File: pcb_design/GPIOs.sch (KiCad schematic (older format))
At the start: 8 parts

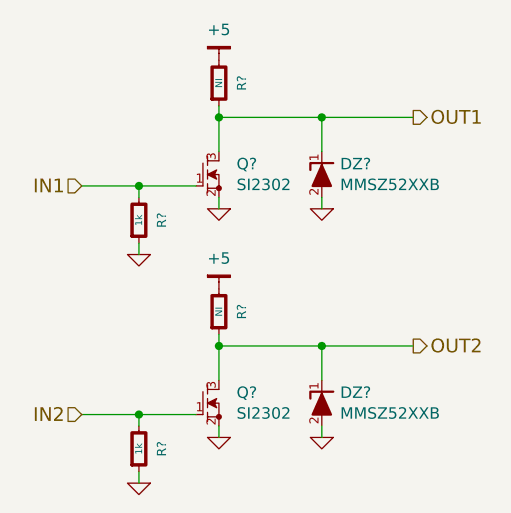
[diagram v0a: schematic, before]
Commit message: Fixed power supply inductor footprints in the layout
Signed-off-by: Marcos Chaparro <mchaparro@paltatech.com>
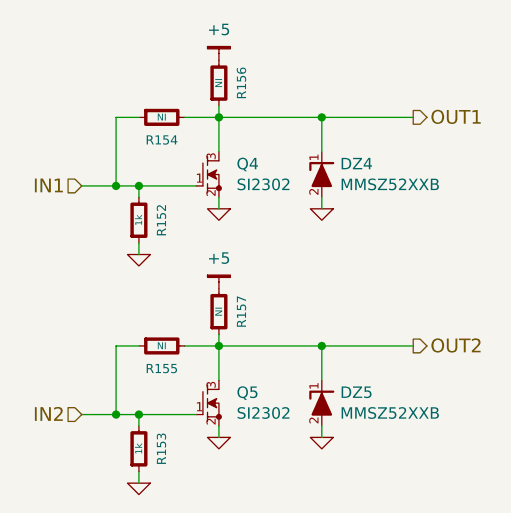
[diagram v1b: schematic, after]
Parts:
- added R154, R155: NI, IPC7351-Nominal:RESC1608X50, symbol R-0603
- gave numbers to parts that had none: 8
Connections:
- net IN1: now also R154.1
- net IN2: now also R155.1
- net OUT1: now also R154.2
- net OUT2: now also R155.2
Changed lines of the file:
@@
 $EndDescr
 $Comp
-L 2N7002K Q?
+L 2N7002K Q5
 U 1 1 594CFF0C
 P 5450 4600
-F 0 "Q?" H 5577 4646 50  0000 L CNN
+F 0 "Q5" H 5577 4646 50  0000 L CNN
 F 1 "SI2302" H 5577 4555 50  0000 L CNN
 F 2 "smd-semi:SOT-23" H 5450 4350 50  0001 C CNN
@@
 $EndComp
 $Comp
-L 2N7002K Q?
+L 2N7002K Q4
 U 1 1 594CFF16
 P 5450 3600
-F 0 "Q?" H 5577 3646 50  0000 L CNN
+F 0 "Q4" H 5577 3646 50  0000 L CNN
 F 1 "SI2302" H 5577 3555 50  0000 L CNN
 F 2 "smd-semi:SOT-23" H 5450 3350 50  0001 C CNN
@@
 P 5500 3750
 AR Path="/594CFF1D" Ref="#PWR?"  Part="1"
-AR Path="/594CEEA9/594CFF1D" Ref="#PWR?"  Part="1"
-F 0 "#PWR?" H 5500 3750 30  0001 C CNN
+AR Path="/594CEEA9/594CFF1D" Ref="#PWR0230"  Part="1"
+F 0 "#PWR0230" H 5500 3750 30  0001 C CNN
 F 1 "GND" H 5500 3680 30  0001 C CNN
 F 2 "" H 5500 3750 60  0000 C CNN
@@
 	5500 4300 5500 4500
 Wire Wire Line
-	5500 4350 6350 4350
+	5350 4350 6350 4350
 Wire Wire Line
 	4900 3650 5400 3650
@@
 P 5500 4750
 AR Path="/594CFF2B" Ref="#PWR?"  Part="1"
-AR Path="/594CEEA9/594CFF2B" Ref="#PWR?"  Part="1"
-F 0 "#PWR?" H 5500 4750 30  0001 C CNN
+AR Path="/594CEEA9/594CFF2B" Ref="#PWR0231"  Part="1"
+F 0 "#PWR0231" H 5500 4750 30  0001 C CNN
 F 1 "GND" H 5500 4680 30  0001 C CNN
 F 2 "" H 5500 4750 60  0000 C CNN
@@
 P 5150 4800
 AR Path="/594CFF3A" Ref="R?"  Part="1"
-AR Path="/594CEEA9/594CFF3A" Ref="R?"  Part="1"
-F 0 "R?" V 5250 4800 40  0000 C CNN
+AR Path="/594CEEA9/594CFF3A" Ref="R153"  Part="1"
+F 0 "R153" V 5250 4800 40  0000 C CNN
 F 1 "1k" V 5150 4800 30  0000 C CNN
 F 2 "IPC7351-Nominal:RESC1608X50" V 5080 4800 30  0001 C CNN
@@
 $EndComp
 $Comp
-L R-0603 R?
+L R-0603 R152
 U 1 1 594CFF46
 P 5150 3800
-F 0 "R?" V 5250 3800 40  0000 C CNN
+F 0 "R152" V 5250 3800 40  0000 C CNN
 F 1 "1k" V 5150 3800 30  0000 C CNN
 F 2 "IPC7351-Nominal:RESC1608X50" V 5080 3800 30  0001 C CNN
@@
 	5150 4900 5150 4950
 $Comp
-L GND #PWR?
+L GND #PWR0232
 U 1 1 594CFF53
 P 5150 3950
-F 0 "#PWR?" H 5150 3950 30  0001 C CNN
+F 0 "#PWR0232" H 5150 3950 30  0001 C CNN
 F 1 "GND" H 5150 3880 30  0001 C CNN
 F 2 "" H 5150 3950 60  0000 C CNN
@@
 $EndComp
 $Comp
-L GND #PWR?
+L GND #PWR0233
 U 1 1 594CFF59
 P 5150 4950
-F 0 "#PWR?" H 5150 4950 30  0001 C CNN
+F 0 "#PWR0233" H 5150 4950 30  0001 C CNN
 F 1 "GND" H 5150 4880 30  0001 C CNN
 F 2 "" H 5150 4950 60  0000 C CNN
@@
 Connection ~ 5150 4650
 $Comp
-L MMSZ52XXB DZ?
+L MMSZ52XXB DZ5
 U 1 1 594D023F
 P 5950 4600
-F 0 "DZ?" H 6030 4646 50  0000 L CNN
+F 0 "DZ5" H 6030 4646 50  0000 L CNN
 F 1 "MMSZ52XXB" H 6030 4555 50  0000 L CNN
 F 2 "smd-semi:SOD-123" H 5950 4450 50  0001 C CNN
@@
 $EndComp
 $Comp
-L MMSZ52XXB DZ?
+L MMSZ52XXB DZ4
 U 1 1 594D026F
 P 5950 3600
-F 0 "DZ?" H 6030 3646 50  0000 L CNN
+F 0 "DZ4" H 6030 3646 50  0000 L CNN
 F 1 "MMSZ52XXB" H 6030 3555 50  0000 L CNN
 F 2 "smd-semi:SOD-123" H 5950 3450 50  0001 C CNN
@@
 P 5950 4750
 AR Path="/594D02CD" Ref="#PWR?"  Part="1"
-AR Path="/594CEEA9/594D02CD" Ref="#PWR?"  Part="1"
-F 0 "#PWR?" H 5950 4750 30  0001 C CNN
+AR Path="/594CEEA9/594D02CD" Ref="#PWR0234"  Part="1"
+F 0 "#PWR0234" H 5950 4750 30  0001 C CNN
 F 1 "GND" H 5950 4680 30  0001 C CNN
 F 2 "" H 5950 4750 60  0000 C CNN
@@
 	5500 3300 5500 3500
 Wire Wire Line
-	5500 3350 6350 3350
+	5350 3350 6350 3350
 Wire Wire Line
 	5950 3350 5950 3500
@@
 P 5950 3750
 AR Path="/594D0367" Ref="#PWR?"  Part="1"
-AR Path="/594CEEA9/594D0367" Ref="#PWR?"  Part="1"
-F 0 "#PWR?" H 5950 3750 30  0001 C CNN
+AR Path="/594CEEA9/594D0367" Ref="#PWR0235"  Part="1"
+F 0 "#PWR0235" H 5950 3750 30  0001 C CNN
 F 1 "GND" H 5950 3680 30  0001 C CNN
 F 2 "" H 5950 3750 60  0000 C CNN
@@
 P 5500 4200
 AR Path="/594D03DA" Ref="R?"  Part="1"
-AR Path="/594CEEA9/594D03DA" Ref="R?"  Part="1"
-F 0 "R?" V 5600 4200 40  0000 C CNN
+AR Path="/594CEEA9/594D03DA" Ref="R157"  Part="1"
+F 0 "R157" V 5600 4200 40  0000 C CNN
 F 1 "NI" V 5500 4200 30  0000 C CNN
 F 2 "IPC7351-Nominal:RESC1608X50" V 5430 4200 30  0001 C CNN
@@
 Connection ~ 5500 4350
 $Comp
-L +5 #PWR?
+L +5 #PWR0236
 U 1 1 594D04CE
 P 5500 4100
-F 0 "#PWR?" H 5500 4150 30  0001 C CNN
+F 0 "#PWR0236" H 5500 4150 30  0001 C CNN
 F 1 "+5" H 5500 4233 50  0000 C CNN
 F 2 "" H 5500 4100 60  0000 C CNN
@@
 P 5500 3200
 AR Path="/594D0581" Ref="R?"  Part="1"
-AR Path="/594CEEA9/594D0581" Ref="R?"  Part="1"
-F 0 "R?" V 5600 3200 40  0000 C CNN
+AR Path="/594CEEA9/594D0581" Ref="R156"  Part="1"
+F 0 "R156" V 5600 3200 40  0000 C CNN
 F 1 "NI" V 5500 3200 30  0000 C CNN
 F 2 "IPC7351-Nominal:RESC1608X50" V 5430 3200 30  0001 C CNN
@@
 $EndComp
 $Comp
-L +5 #PWR?
+L +5 #PWR0237
 U 1 1 594D0587
 P 5500 3100
-F 0 "#PWR?" H 5500 3150 30  0001 C CNN
+F 0 "#PWR0237" H 5500 3150 30  0001 C CNN
 F 1 "+5" H 5500 3233 50  0000 C CNN
 F 2 "" H 5500 3100 60  0000 C CNN
@@
 Text HLabel 6350 4350 2    60   Output ~ 0
 OUT2
+$Comp
+L R-0603 R?
+U 1 1 59494773
+P 5250 4350
+AR Path="/59494773" Ref="R?"  Part="1"
+AR Path="/594CEEA9/59494773" Ref="R155"  Part="1"
+F 0 "R155" V 5350 4350 40  0000 C CNN
+F 1 "NI" V 5250 4350 30  0000 C CNN
+F 2 "IPC7351-Nominal:RESC1608X50" V 5180 4350 30  0001 C CNN
+F 3 "" H 5250 4350 30  0001 C CNN
+F 4 "Yageo" H -750 -2300 50  0001 C CNN "MFR"
+F 5 "RC0603FR-071KL" H -750 -2300 50  0001 C CNN "MPN"
+F 6 "Digikey" H -750 -2300 50  0001 C CNN "SPR"
+F 7 "311-1.00KHRCT-ND" H -750 -2300 50  0001 C CNN "SPN"
+F 8 "" H -750 -2300 50  0001 C CNN "SPURL"
+	1    5250 4350
+	0    -1   1    0
+$EndComp
+Wire Wire Line
+	5150 4350 5050 4350
+Wire Wire Line
+	5050 4350 5050 4650
+Connection ~ 5050 4650
+$Comp
+L R-0603 R?
+U 1 1 59494838
+P 5250 3350
+AR Path="/59494838" Ref="R?"  Part="1"
+AR Path="/594CEEA9/59494838" Ref="R154"  Part="1"
+F 0 "R154" V 5350 3350 40  0000 C CNN
+F 1 "NI" V 5250 3350 30  0000 C CNN
+F 2 "IPC7351-Nominal:RESC1608X50" V 5180 3350 30  0001 C CNN
+F 3 "" H 5250 3350 30  0001 C CNN
+F 4 "Yageo" H -750 -3300 50  0001 C CNN "MFR"
+F 5 "RC0603FR-071KL" H -750 -3300 50  0001 C CNN "MPN"
+F 6 "Digikey" H -750 -3300 50  0001 C CNN "SPR"
+F 7 "311-1.00KHRCT-ND" H -750 -3300 50  0001 C CNN "SPN"
+F 8 "" H -750 -3300 50  0001 C CNN "SPURL"
+	1    5250 3350
+	0    -1   1    0
+$EndComp
+Wire Wire Line
+	5150 3350 5050 3350
+Wire Wire Line
+	5050 3350 5050 3650
+Connection ~ 5050 3650
 $EndSCHEMATC

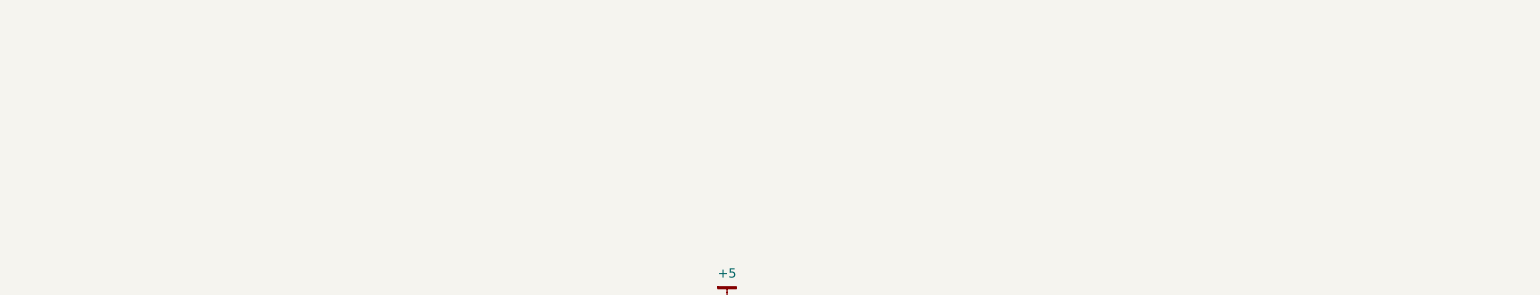
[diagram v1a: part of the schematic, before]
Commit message: Added RC filter to FAULT line to prevent noise triggering it
Signed-off-by: Marcos Chaparro <mchaparro@paltatech.com>
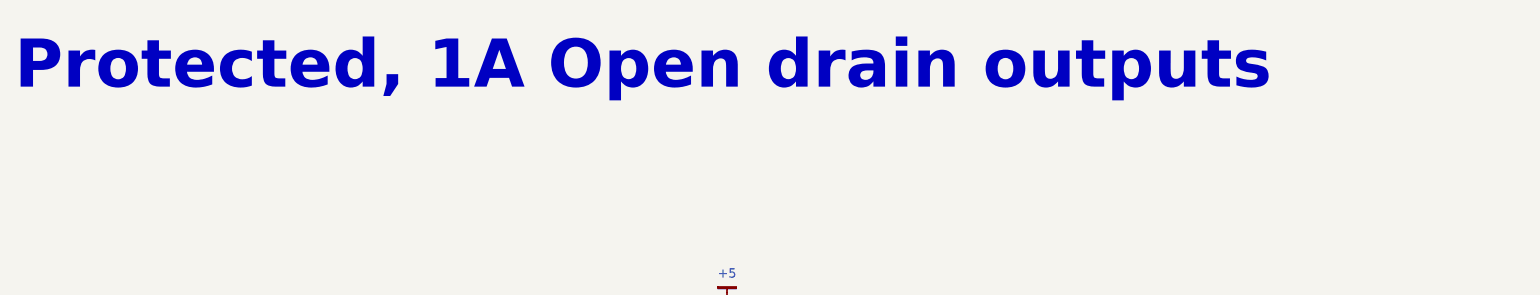
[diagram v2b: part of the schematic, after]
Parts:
- R152, R153: BOM (none) -> RES SMD 1k 5% [0603]
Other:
- note added: "Protected, 1A Open drain outputs"
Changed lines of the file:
@@
 F 7 "311-1.00KHRCT-ND" H -850 -1850 50  0001 C CNN "SPN"
 F 8 "" H -850 -1850 50  0001 C CNN "SPURL"
+F 9 "RES SMD 1k 5% [0603]" H 0   0   60  0001 C CNN "BOM"
 	1    5150 4800
 	1    0    0    1
@@
 F 7 "311-1.00KHRCT-ND" H -850 -2850 50  0001 C CNN "SPN"
 F 8 "" H -850 -2850 50  0001 C CNN "SPURL"
+F 9 "RES SMD 1k 5% [0603]" H 0   0   60  0001 C CNN "BOM"
 	1    5150 3800
 	1    0    0    1
@@
 	5050 3350 5050 3650
 Connection ~ 5050 3650
+Text Notes 1650 2000 0    260  ~ 52
+Protected, 1A Open drain outputs
 $EndSCHEMATC
